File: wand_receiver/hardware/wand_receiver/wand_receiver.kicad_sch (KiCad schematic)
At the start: 53 parts, among them J1 AudioJack2_SwitchT, J1 USB_C_Receptacle_USB2.0, J2 Conn_02x05_Odd_Even, J3 AudioJack2_SwitchT, J4 AudioJack2_SwitchT, Q1 MUN5214DW1T1G, U1 CP2104, U1 R-783.3-1.0, U2 ESP32-PICO-D4, U2 MCP4922-ESL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

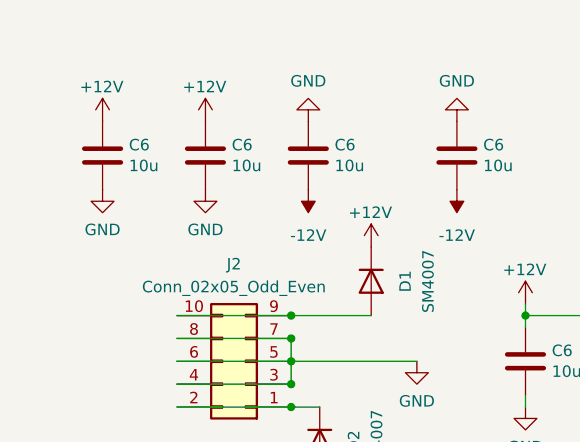
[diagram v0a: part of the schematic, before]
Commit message: Added electrolytic caps
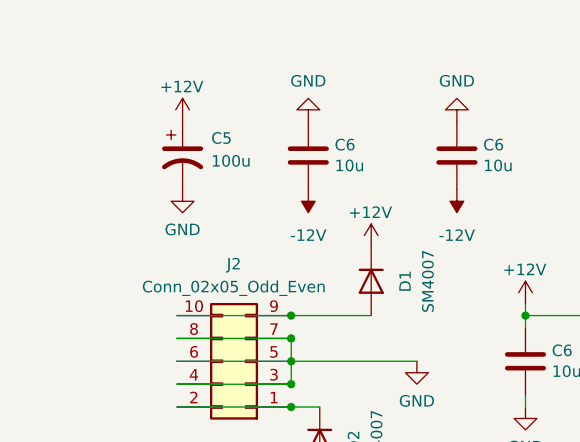
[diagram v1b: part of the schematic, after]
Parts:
- removed C6 (x2): 10u, Capacitor_SMD:C_0603_1608Metric, symbol Device:C
- added C5: 100u, Capacitor_SMD:CP_Elec_6.3x5.4, symbol Device:C_Polarized_US
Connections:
- net +12V: now also C5.1
- net GND: now also C5.2
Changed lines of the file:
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@@
     )
   )
-  (symbol (lib_id "Device:C") (at 30.48 30.48 0) (unit 1)
-    (in_bom yes) (on_board yes) (dnp no)
-    (property "Reference" "C6" (at 33.401 29.3116 0)
-      (effects (font (size 1.27 1.27)) (justify left))
-    )
-    (property "Value" "10u" (at 33.401 31.623 0)
-      (effects (font (size 1.27 1.27)) (justify left))
-    )
-    (property "Footprint" "Capacitor_SMD:C_0603_1608Metric" (at 31.4452 34.29 0)
-      (effects (font (size 1.27 1.27)) hide)
-    )
-    (property "Datasheet" "~" (at 30.48 30.48 0)
-      (effects (font (size 1.27 1.27)) hide)
-    )
-    (pin "1")
-    (pin "2")
-    (instances
-      (project "jukebox_light_controller"
-        (path "/3d7cdb1e-a810-4ff2-a852-82c48438ee64"
-          (reference "C6") (unit 1)
-        )
-      )
-      (project "wand_receiver"
-        (path "/6528a74f-fb83-4bcc-9141-ec4744f78469"
-          (reference "C5") (unit 1)
-        )
-      )
-      (project "laser_controller"
-        (path "/66f4951c-8ca6-44d4-8426-28e02ddf3b18"
-          (reference "C43") (unit 1)
-        )
-      )
-      (project "canbus_adapter"
-        (path "/805386a4-6883-4c41-8ba1-2a13d67886f6"
-          (reference "C3") (unit 1)
-        )
-      )
-      (project "RP2040_minimal"
-        (path "/82a49de2-ec1b-43dd-97fe-0b636089eb84"
-          (reference "C1") (unit 1)
-        )
-      )
-      (project "combo_laser_driver"
-        (path "/e63e39d7-6ac0-4ffd-8aa3-1841a4541b55"
-          (reference "C2") (unit 1)
-        )
-      )
-    )
-  )
   (symbol (lib_id "Device:R_US") (at 213.995 72.39 0) (unit 1)
     (in_bom yes) (on_board yes) (dnp no) (fields_autoplaced)
@@
     )
   )
-  (symbol (lib_id "PCM_4ms_Power-symbol:+12V") (at 30.48 26.67 0) (unit 1)
+  (symbol (lib_id "PCM_4ms_Power-symbol:+12V") (at 39.37 26.67 0) (unit 1)
     (in_bom yes) (on_board yes) (dnp no)
-    (property "Reference" "#PWR049" (at 30.48 30.48 0)
+    (property "Reference" "#PWR049" (at 39.37 30.48 0)
       (effects (font (size 1.27 1.27)) hide)
     )
-    (property "Value" "+12V" (at 27.94 22.86 0)
+    (property "Value" "+12V" (at 36.83 22.86 0)
       (effects (font (size 1.27 1.27)) (justify left))
     )
-    (property "Footprint" "" (at 30.48 26.67 0)
+    (property "Footprint" "" (at 39.37 26.67 0)
       (effects (font (size 1.27 1.27)) hide)
     )
-    (property "Datasheet" "" (at 30.48 26.67 0)
+    (property "Datasheet" "" (at 39.37 26.67 0)
       (effects (font (size 1.27 1.27)) hide)
     )
@@
     )
   )
-  (symbol (lib_id "PCM_4ms_Power-symbol:+12V") (at 41.91 26.67 0) (unit 1)
-    (in_bom yes) (on_board yes) (dnp no)
-    (property "Reference" "#PWR049" (at 41.91 30.48 0)
-      (effects (font (size 1.27 1.27)) hide)
-    )
-    (property "Value" "+12V" (at 39.37 22.86 0)
-      (effects (font (size 1.27 1.27)) (justify left))
-    )
-    (property "Footprint" "" (at 41.91 26.67 0)
-      (effects (font (size 1.27 1.27)) hide)
-    )
-    (property "Datasheet" "" (at 41.91 26.67 0)
-      (effects (font (size 1.27 1.27)) hide)
-    )
-    (pin "1")
-    (instances
-      (project "jukebox_light_controller"
-        (path "/3d7cdb1e-a810-4ff2-a852-82c48438ee64"
-          (reference "#PWR049") (unit 1)
-        )
-      )
-      (project "wand_receiver"
-        (path "/6528a74f-fb83-4bcc-9141-ec4744f78469"
-          (reference "#PWR02") (unit 1)
-        )
-      )
-      (project "laser_controller"
-        (path "/66f4951c-8ca6-44d4-8426-28e02ddf3b18"
-          (reference "#PWR035") (unit 1)
-        )
-      )
-      (project "canbus_adapter"
-        (path "/805386a4-6883-4c41-8ba1-2a13d67886f6"
-          (reference "#PWR094") (unit 1)
-        )
-      )
-      (project "combo_laser_driver"
-        (path "/e63e39d7-6ac0-4ffd-8aa3-1841a4541b55"
-          (reference "#PWR032") (unit 1)
-        )
-      )
-    )
-  )
   (symbol (lib_id "RF_Module:ESP32-PICO-D4") (at 244.475 111.76 0) (unit 1)
     (in_bom yes) (on_board yes) (dnp no) (fields_autoplaced)
@@
     )
   )
-  (symbol (lib_id "Device:C") (at 41.91 30.48 0) (unit 1)
-    (in_bom yes) (on_board yes) (dnp no)
-    (property "Reference" "C6" (at 44.831 29.3116 0)
-      (effects (font (size 1.27 1.27)) (justify left))
-    )
-    (property "Value" "10u" (at 44.831 31.623 0)
-      (effects (font (size 1.27 1.27)) (justify left))
-    )
-    (property "Footprint" "Capacitor_SMD:C_0603_1608Metric" (at 42.8752 34.29 0)
-      (effects (font (size 1.27 1.27)) hide)
-    )
-    (property "Datasheet" "~" (at 41.91 30.48 0)
-      (effects (font (size 1.27 1.27)) hide)
-    )
-    (pin "1")
-    (pin "2")
-    (instances
-      (project "jukebox_light_controller"
-        (path "/3d7cdb1e-a810-4ff2-a852-82c48438ee64"
-          (reference "C6") (unit 1)
-        )
-      )
-      (project "wand_receiver"
-        (path "/6528a74f-fb83-4bcc-9141-ec4744f78469"
-          (reference "C6") (unit 1)
-        )
-      )
-      (project "laser_controller"
-        (path "/66f4951c-8ca6-44d4-8426-28e02ddf3b18"
-          (reference "C46") (unit 1)
-        )
-      )
-      (project "canbus_adapter"
-        (path "/805386a4-6883-4c41-8ba1-2a13d67886f6"
-          (reference "C3") (unit 1)
-        )
-      )
-      (project "RP2040_minimal"
-        (path "/82a49de2-ec1b-43dd-97fe-0b636089eb84"
-          (reference "C1") (unit 1)
-        )
-      )
-      (project "combo_laser_driver"
-        (path "/e63e39d7-6ac0-4ffd-8aa3-1841a4541b55"
-          (reference "C2") (unit 1)
-        )
-      )
-    )
-  )
   (symbol (lib_id "Device:R_US") (at 135.255 53.34 270) (unit 1)
     (in_bom yes) (on_board yes) (dnp no)
@@
     )
   )
+  (symbol (lib_id "Device:C_Polarized_US") (at 39.37 30.48 0) (unit 1)
+    (in_bom yes) (on_board yes) (dnp no) (fields_autoplaced)
+    (property "Reference" "C5" (at 42.545 28.575 0)
+      (effects (font (size 1.27 1.27)) (justify left))
+    )
+    (property "Value" "100u" (at 42.545 31.115 0)
+      (effects (font (size 1.27 1.27)) (justify left))
+    )
+    (property "Footprint" "Capacitor_SMD:CP_Elec_6.3x5.4" (at 39.37 30.48 0)
+      (effects (font (size 1.27 1.27)) hide)
+    )
+    (property "Datasheet" "~" (at 39.37 30.48 0)
+      (effects (font (size 1.27 1.27)) hide)
+    )
+    (pin "1")
+    (pin "2")
+    (instances
+      (project "wand_receiver"
+        (path "/6528a74f-fb83-4bcc-9141-ec4744f78469"
+          (reference "C5") (unit 1)
+        )
+      )
+      (project "laser_controller"
+        (path "/66f4951c-8ca6-44d4-8426-28e02ddf3b18"
+          (reference "C49") (unit 1)
+        )
+      )
+    )
+  )
   (symbol (lib_id "Connector:USB_C_Receptacle_USB2.0") (at 38.735 146.05 0) (unit 1)
     (in_bom yes) (on_board yes) (dnp no) (fields_autoplaced)
@@
     )
   )
-  (symbol (lib_id "power:GND") (at 30.48 34.29 0) (unit 1)
+  (symbol (lib_id "power:GND") (at 39.37 34.29 0) (unit 1)
     (in_bom yes) (on_board yes) (dnp no)
-    (property "Reference" "#PWR044" (at 30.48 40.64 0)
+    (property "Reference" "#PWR044" (at 39.37 40.64 0)
       (effects (font (size 1.27 1.27)) hide)
     )
-    (property "Value" "GND" (at 30.48 38.735 0)
+    (property "Value" "GND" (at 39.37 38.735 0)
       (effects (font (size 1.27 1.27)))
     )
-    (property "Footprint" "" (at 30.48 34.29 0)
+    (property "Footprint" "" (at 39.37 34.29 0)
       (effects (font (size 1.27 1.27)) hide)
     )
-    (property "Datasheet" "" (at 30.48 34.29 0)
+    (property "Datasheet" "" (at 39.37 34.29 0)
       (effects (font (size 1.27 1.27)) hide)
     )
@@
         )
       )
-    )
-  )
-  (symbol (lib_id "power:GND") (at 41.91 34.29 0) (unit 1)
-    (in_bom yes) (on_board yes) (dnp no)
-    (property "Reference" "#PWR044" (at 41.91 40.64 0)
-      (effects (font (size 1.27 1.27)) hide)
-    )
-    (property "Value" "GND" (at 41.91 38.735 0)
-      (effects (font (size 1.27 1.27)))
-    )
-    (property "Footprint" "" (at 41.91 34.29 0)
-      (effects (font (size 1.27 1.27)) hide)
-    )
-    (property "Datasheet" "" (at 41.91 34.29 0)
-      (effects (font (size 1.27 1.27)) hide)
-    )
-    (pin "1")
-    (instances
-      (project "jukebox_light_controller"
-        (path "/3d7cdb1e-a810-4ff2-a852-82c48438ee64"
-          (reference "#PWR044") (unit 1)
-        )
-      )
-      (project "wand_receiver"
-        (path "/6528a74f-fb83-4bcc-9141-ec4744f78469"
-          (reference "#PWR010") (unit 1)
-        )
-      )
-      (project "laser_controller"
-        (path "/66f4951c-8ca6-44d4-8426-28e02ddf3b18"
-          (reference "#PWR036") (unit 1)
-        )
-      )
-      (project "canbus_adapter"
-        (path "/805386a4-6883-4c41-8ba1-2a13d67886f6"
-          (reference "#PWR014") (unit 1)
-        )
-      )
-      (project "RP2040_minimal"
-        (path "/82a49de2-ec1b-43dd-97fe-0b636089eb84"
-          (reference "#PWR05") (unit 1)
-        )
-      )
-      (project "combo_laser_driver"
-        (path "/e63e39d7-6ac0-4ffd-8aa3-1841a4541b55"
-          (reference "#PWR029") (unit 1)
-        )
-      )
